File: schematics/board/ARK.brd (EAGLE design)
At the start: 89.6 x 89 mm, 199 parts, among them IC1 STM32F103C8T, Q5 8MHz

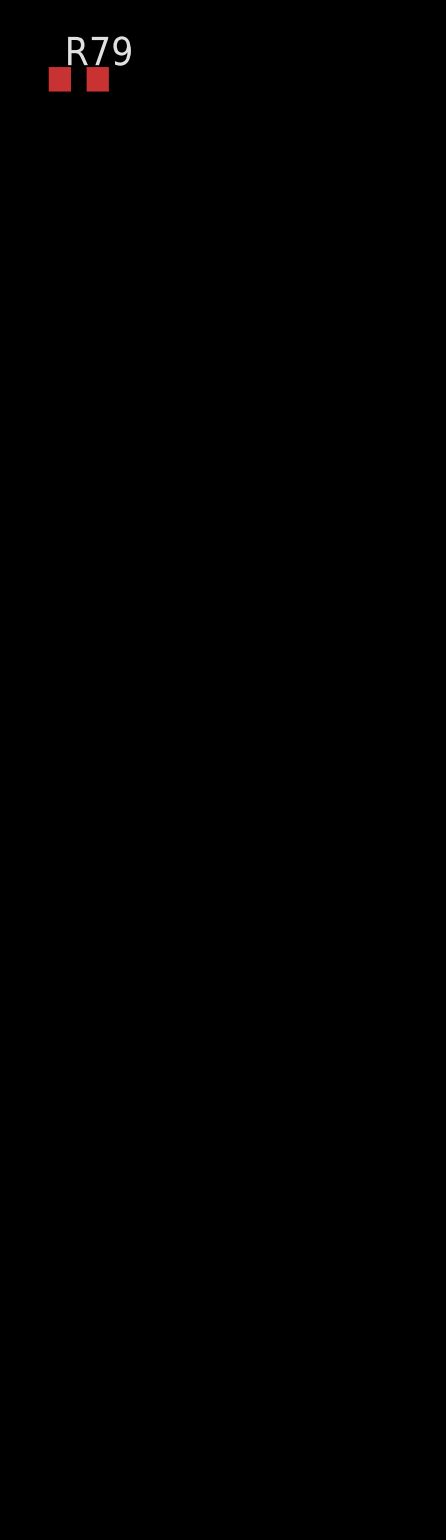
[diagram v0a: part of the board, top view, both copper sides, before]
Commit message: изменения схемы АРК
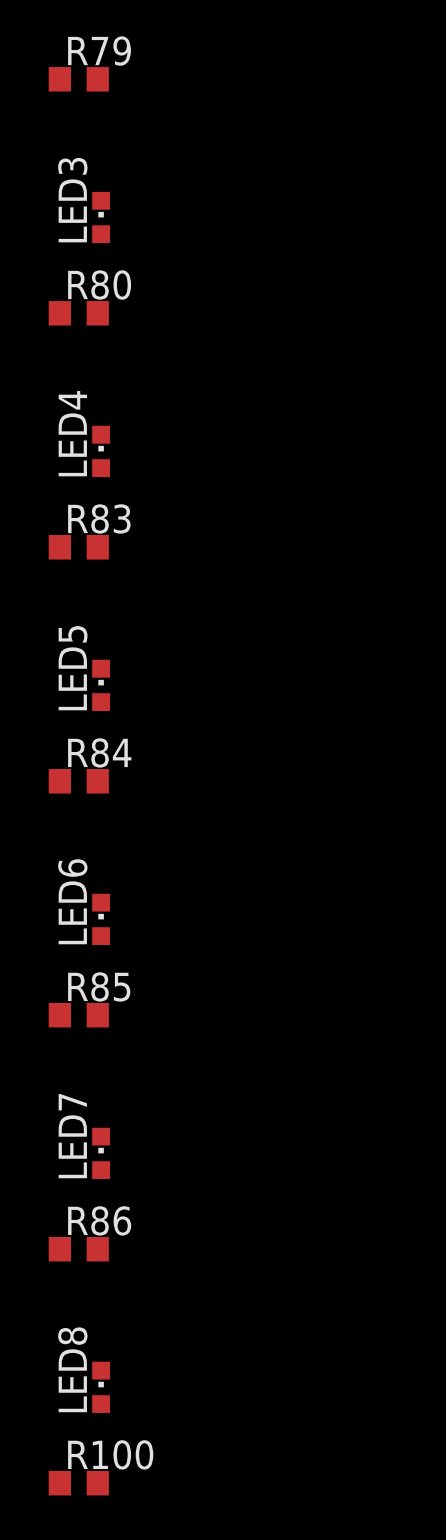
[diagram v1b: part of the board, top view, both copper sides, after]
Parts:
- added LED3, LED4, LED5, LED6, LED7, LED8: (no value), led:CHIPLED_0603
- added R100, R80, R83, R84, R85, R86: 1k2, resistor:R0603
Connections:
- net N$138 renamed 90
- new net N$25: R70.1, U$60.2
- new net N$5: R30.1, U$22.2
- new net N$54: LED3.A, R80.2
- new net N$56: LED4.A, R83.2
- new net N$57: LED5.A, R84.2
- new net N$58: LED6.A, R85.2
- new net N$59: LED7.A, R86.2
- new net N$60: LED8.A, R100.2
- net B-1: now also R86.1
- net B-2: now also R100.1
- net B-3: now also R84.1
- net B-4: now also R85.1
- net B-5: now also R83.1
- net B-6: now also R80.1
- net BUSPLUS: now also LED3.C, LED4.C, LED5.C, LED6.C, LED7.C, LED8.C
- net GND: now also U$22.10; no longer R30.1, R70.1, U$22.2, U$60.2
- net N$26: now also U$22.1
- net VDD: no longer U$22.1, U$22.10

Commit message: доработаны схемы БСК1 и БКУ
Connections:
- net GND: now also U$23.GND0, U$23.GND1; no longer U$23.P$12, U$23.P$9
- net RES-C: now also U$23.RESET/EN; no longer U$23.P$6
- net RX-C: now also U$23.RX0/M1; no longer U$23.P$11
- net SWC: now also U$23.SWC/TXD; no longer U$23.P$5
- net SWD: now also U$23.SWD/RXD; no longer U$23.P$4
- net TX-C: now also U$23.TX0/3V3; no longer U$23.P$10
- net VDD: now also U$23.3V3; no longer U$23.P$2, U$23.P$7
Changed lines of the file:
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@@
 <contactref element="VAR5B" pad="3"/>
 <contactref element="VAR5A" pad="3"/>
-<contactref element="U$23" pad="P$2"/>
-<contactref element="U$23" pad="P$7"/>
 <contactref element="R25" pad="1"/>
 <contactref element="R26" pad="1"/>
@@
 <contactref element="R64" pad="1"/>
 <contactref element="R79" pad="1"/>
+<contactref element="U$23" pad="3V3"/>
 <wire x1="40.69" y1="73.8" x2="65.69" y2="73.8" width="0" layer="19" extent="1-1"/>
 <wire x1="15.69" y1="73.8" x2="40.69" y2="73.8" width="0" layer="19" extent="1-1"/>
@@
 <wire x1="24.47" y1="25.1" x2="23.18" y2="40.7" width="0" layer="19" extent="1-1"/>
 <wire x1="41.31" y1="15.2" x2="24.47" y2="25.1" width="0" layer="19" extent="1-1"/>
-<wire x1="54.25" y1="12.1" x2="41.31" y2="15.2" width="0" layer="19" extent="1-1"/>
-<wire x1="56.75" y1="12.1" x2="54.25" y2="12.1" width="0" layer="19" extent="1-1"/>
-<wire x1="67.55" y1="14.65" x2="56.75" y2="12.1" width="0" layer="19" extent="1-1"/>
+<wire x1="54.75" y1="12.1" x2="41.31" y2="15.2" width="0" layer="19" extent="1-1"/>
+<wire x1="67.55" y1="14.65" x2="54.75" y2="12.1" width="0" layer="19" extent="1-1"/>
 <wire x1="73.05" y1="13.15" x2="67.55" y2="14.65" width="0" layer="19" extent="1-1"/>
 <wire x1="69.05" y1="21.65" x2="67.55" y2="14.65" width="0" layer="19" extent="1-1"/>
@@
 <wire x1="86.85" y1="18.9" x2="81.9" y2="25.55" width="0" layer="19" extent="1-1"/>
 <wire x1="86.85" y1="17.8" x2="86.85" y2="18.9" width="0" layer="19" extent="1-1"/>
-<wire x1="-24.7" y1="-300.97" x2="54.25" y2="12.1" width="0" layer="19" extent="1-1"/>
+<wire x1="-24.7" y1="-300.97" x2="41.31" y2="15.2" width="0" layer="19" extent="1-1"/>
 <wire x1="-28.7" y1="-300.97" x2="-24.7" y2="-300.97" width="0" layer="19" extent="1-1"/>
 <wire x1="-31.3" y1="-299.68" x2="-28.7" y2="-300.97" width="0" layer="19" extent="1-1"/>
@@
 <contactref element="R62" pad="1"/>
 <contactref element="R82" pad="1"/>
-<contactref element="U$23" pad="P$12" route="any" routetag="G$1.GND"/>
-<contactref element="U$23" pad="P$9" route="any" routetag="G$1.GND"/>
 <contactref element="U$24" pad="23"/>
 <contactref element="U$15" pad="23"/>
@@
 <contactref element="VAR5A" pad="4"/>
 <contactref element="U$22" pad="10"/>
+<contactref element="U$23" pad="GND0"/>
+<contactref element="U$23" pad="GND1"/>
 <wire x1="71.6" y1="55.4" x2="68.23" y2="73.8" width="0" layer="19" extent="1-1"/>
 <wire x1="59.3" y1="55.4" x2="71.6" y2="55.4" width="0" layer="19" extent="1-1"/>
@@
 <wire x1="18.23" y1="73.8" x2="21.6" y2="55.4" width="0" layer="19" extent="1-1"/>
 <wire x1="52.3" y1="12.1" x2="30.3" y2="19.8" width="0" layer="19" extent="1-1"/>
+<wire x1="58.7" y1="12.1" x2="52.3" y2="12.1" width="0" layer="19" extent="1-1"/>
 <wire x1="72.55" y1="13.15" x2="58.7" y2="12.1" width="0" layer="19" extent="1-1"/>
 <wire x1="71.7" y1="25.65" x2="72.55" y2="13.15" width="0" layer="19" extent="1-1"/>
@@
 </signal>
 <signal name="SWC">
-<contactref element="U$23" pad="P$5"/>
 <contactref element="IC1" pad="37"/>
 <contactref element="R27" pad="2"/>
+<contactref element="U$23" pad="SWC/TXD"/>
 <wire x1="67.55" y1="20.15" x2="81.9" y2="23.85" width="0" layer="19" extent="1-1"/>
 <wire x1="55.75" y1="12.1" x2="67.55" y2="20.15" width="0" layer="19" extent="1-1"/>
 </signal>
 <signal name="SWD">
-<contactref element="U$23" pad="P$4"/>
 <contactref element="IC1" pad="34"/>
 <contactref element="R64" pad="2"/>
+<contactref element="U$23" pad="SWD/RXD"/>
 <wire x1="70.05" y1="21.65" x2="81.9" y2="28.75" width="0" layer="19" extent="1-1"/>
 <wire x1="55.25" y1="12.1" x2="70.05" y2="21.65" width="0" layer="19" extent="1-1"/>
 </signal>
 <signal name="TX-C">
-<contactref element="U$23" pad="P$10"/>
 <contactref element="IC1" pad="30"/>
-<wire x1="53.1" y1="12.1" x2="72.05" y2="21.65" width="0" layer="19" extent="1-1"/>
+<contactref element="U$23" pad="TX0/3V3"/>
+<wire x1="57.25" y1="12.1" x2="72.05" y2="21.65" width="0" layer="19" extent="1-1"/>
 </signal>
 <signal name="RX-C">
-<contactref element="U$23" pad="P$11"/>
 <contactref element="IC1" pad="31"/>
-<wire x1="57.9" y1="12.1" x2="71.55" y2="21.65" width="0" layer="19" extent="1-1"/>
+<contactref element="U$23" pad="RX0/M1"/>
+<wire x1="53.75" y1="12.1" x2="71.55" y2="21.65" width="0" layer="19" extent="1-1"/>
 </signal>
 <signal name="RES-C">
-<contactref element="U$23" pad="P$6"/>
 <contactref element="IC1" pad="7"/>
 <contactref element="R79" pad="2"/>
-<wire x1="56.25" y1="12.1" x2="-54.15" y2="-330.9" width="0" layer="19" extent="1-1"/>
-<wire x1="72.05" y1="13.15" x2="56.25" y2="12.1" width="0" layer="19" extent="1-1"/>
+<contactref element="U$23" pad="RESET/EN"/>
+<wire x1="53.1" y1="12.1" x2="-54.15" y2="-330.9" width="0" layer="19" extent="1-1"/>
+<wire x1="72.05" y1="13.15" x2="53.1" y2="12.1" width="0" layer="19" extent="1-1"/>
 </signal>
 <signal name="N$5">

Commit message: обновлена схема БКУ
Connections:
- removed net RES-C: IC1.7, R79.2, U$23.RESET/EN
- new net NRST: IC1.7, R79.2, U$23.NRST/EN
- net RX-C: now also U$23.RX0; no longer U$23.RX0/M1
- net TX-C: now also U$23.TX0; no longer U$23.TX0/3V3
- net VDD: now also U$23.3V3/BUS0, U$23.3V3/BUS1; no longer U$23.3V3
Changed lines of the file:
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@@
 <contactref element="R64" pad="1"/>
 <contactref element="R79" pad="1"/>
-<contactref element="U$23" pad="3V3"/>
+<contactref element="U$23" pad="3V3/BUS1"/>
+<contactref element="U$23" pad="3V3/BUS0"/>
 <wire x1="40.69" y1="73.8" x2="65.69" y2="73.8" width="0" layer="19" extent="1-1"/>
 <wire x1="15.69" y1="73.8" x2="40.69" y2="73.8" width="0" layer="19" extent="1-1"/>
@@
 <wire x1="24.47" y1="25.1" x2="23.18" y2="40.7" width="0" layer="19" extent="1-1"/>
 <wire x1="41.31" y1="15.2" x2="24.47" y2="25.1" width="0" layer="19" extent="1-1"/>
-<wire x1="54.75" y1="12.1" x2="41.31" y2="15.2" width="0" layer="19" extent="1-1"/>
-<wire x1="67.55" y1="14.65" x2="54.75" y2="12.1" width="0" layer="19" extent="1-1"/>
+<wire x1="54.25" y1="12.1" x2="41.31" y2="15.2" width="0" layer="19" extent="1-1"/>
+<wire x1="56.75" y1="12.1" x2="54.25" y2="12.1" width="0" layer="19" extent="1-1"/>
+<wire x1="67.55" y1="14.65" x2="56.75" y2="12.1" width="0" layer="19" extent="1-1"/>
 <wire x1="73.05" y1="13.15" x2="67.55" y2="14.65" width="0" layer="19" extent="1-1"/>
 <wire x1="69.05" y1="21.65" x2="67.55" y2="14.65" width="0" layer="19" extent="1-1"/>
@@
 <wire x1="86.85" y1="18.9" x2="81.9" y2="25.55" width="0" layer="19" extent="1-1"/>
 <wire x1="86.85" y1="17.8" x2="86.85" y2="18.9" width="0" layer="19" extent="1-1"/>
-<wire x1="-24.7" y1="-300.97" x2="41.31" y2="15.2" width="0" layer="19" extent="1-1"/>
+<wire x1="-24.7" y1="-300.97" x2="54.25" y2="12.1" width="0" layer="19" extent="1-1"/>
 <wire x1="-28.7" y1="-300.97" x2="-24.7" y2="-300.97" width="0" layer="19" extent="1-1"/>
 <wire x1="-31.3" y1="-299.68" x2="-28.7" y2="-300.97" width="0" layer="19" extent="1-1"/>
@@
 <signal name="TX-C">
 <contactref element="IC1" pad="30"/>
-<contactref element="U$23" pad="TX0/3V3"/>
+<contactref element="U$23" pad="TX0"/>
 <wire x1="57.25" y1="12.1" x2="72.05" y2="21.65" width="0" layer="19" extent="1-1"/>
 </signal>
 <signal name="RX-C">
 <contactref element="IC1" pad="31"/>
-<contactref element="U$23" pad="RX0/M1"/>
+<contactref element="U$23" pad="RX0"/>
 <wire x1="53.75" y1="12.1" x2="71.55" y2="21.65" width="0" layer="19" extent="1-1"/>
 </signal>
-<signal name="RES-C">
+<signal name="NRST">
 <contactref element="IC1" pad="7"/>
 <contactref element="R79" pad="2"/>
-<contactref element="U$23" pad="RESET/EN"/>
+<contactref element="U$23" pad="NRST/EN"/>
 <wire x1="53.1" y1="12.1" x2="-54.15" y2="-330.9" width="0" layer="19" extent="1-1"/>
 <wire x1="72.05" y1="13.15" x2="53.1" y2="12.1" width="0" layer="19" extent="1-1"/>

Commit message: Добавлены светодиоды на платы БСК
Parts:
- added C32, C51: 0,1µ, rcl:C0603
- added C43, C52: 10µ, rcl:C1206
- C30, C36, C38: device rcl:C1206 -> rcl:C0603
- R30: value ? -> 150k
- R61: value ? -> 680k
- R70: value 51k -> 150k
- R83: value 1k2 -> 2k
- moved R100 409.9 mm to (18.5, 9.40), turned to 90 degrees
- moved LED8 405.8 mm to (14.2, 10.4), turned to 90 degrees
- moved R86 395.9 mm to (20.0, 5.30), turned to 90 degrees
- moved LED7 391.7 mm to (15.7, 6.30), turned to 90 degrees
- moved R63 386.4 mm to (75.2, 37.8), turned to 180 degrees
- moved R85 381.6 mm to (12.3, 2.70), turned to 90 degrees
- moved R84 380.1 mm to (27.9, 8.50), turned to 90 degrees
- moved LED6 377.4 mm to (8.00, 3.70), turned to 90 degrees
- moved LED5 375.7 mm to (23.6, 9.50), turned to 90 degrees
- moved R79 370.6 mm to (78.4, 14.9)
- moved R32 365.5 mm to (67.7, 45.0), turned to 180 degrees
- moved R83 364.1 mm to (8.60, 6.60), turned to 90 degrees
- moved LED4 360.0 mm to (4.30, 7.60), turned to 90 degrees
- moved R57 358.2 mm to (67.7, 39.0), turned to 180 degrees
- moved R80 357.7 mm to (9.00, 10.5), turned to 90 degrees
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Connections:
- removed net N$26: C31.1, U$16.11, U$16.15, U$16.16, U$22.1
- removed net RESET: IC1.28, U$22.7, U$60.7
- new net DPC_RST: IC1.27, U$60.7
- new net DPD_RST: IC1.28, U$22.7
- net BUSPLUS: no longer LED4.C
- net GND: now also C32.2, C43.2, C51.2, C52.2
- net N$25: now also C32.1, C43.1, U$60.1
- net N$5: now also C51.1, C52.1, U$22.1
- net VDD: now also C31.1, LED4.C, U$16.11, U$16.15, U$16.16; no longer U$60.1

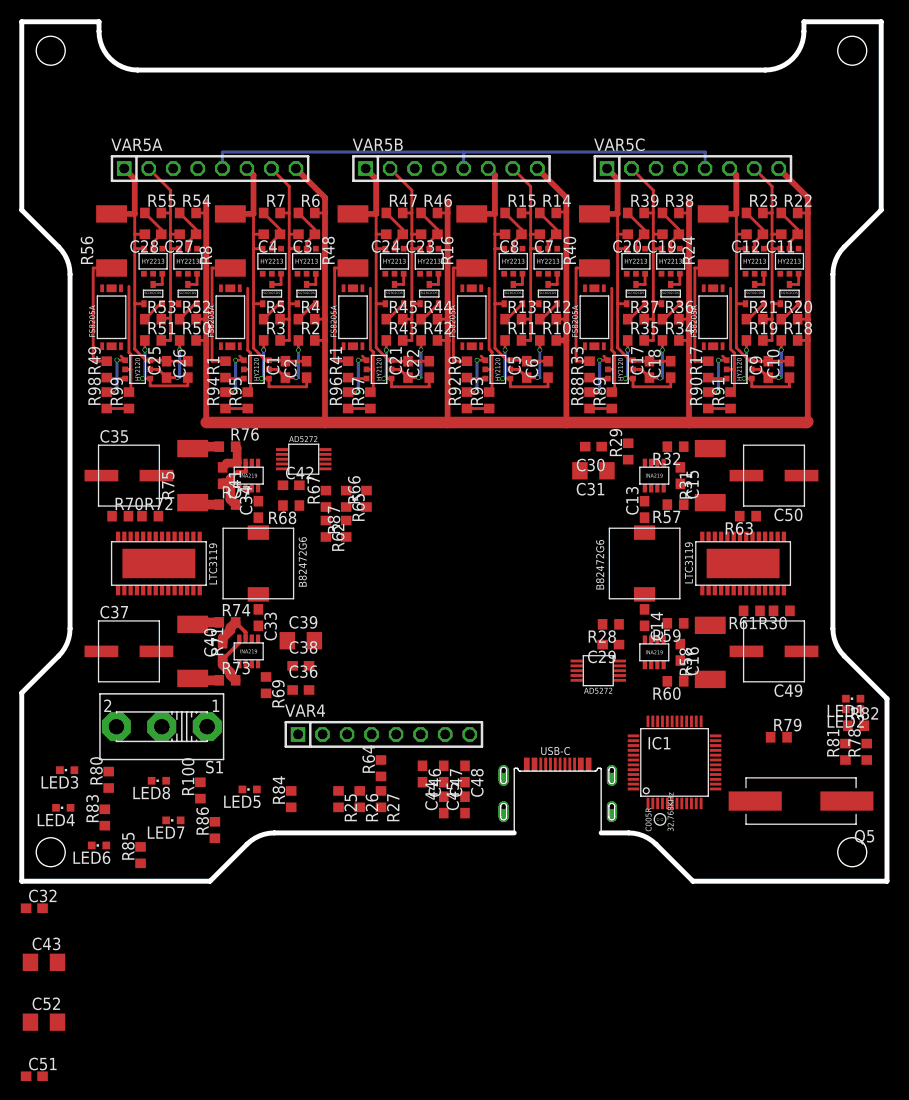
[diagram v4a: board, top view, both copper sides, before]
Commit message: Незначительные изменения в платах БСК1 и АРК
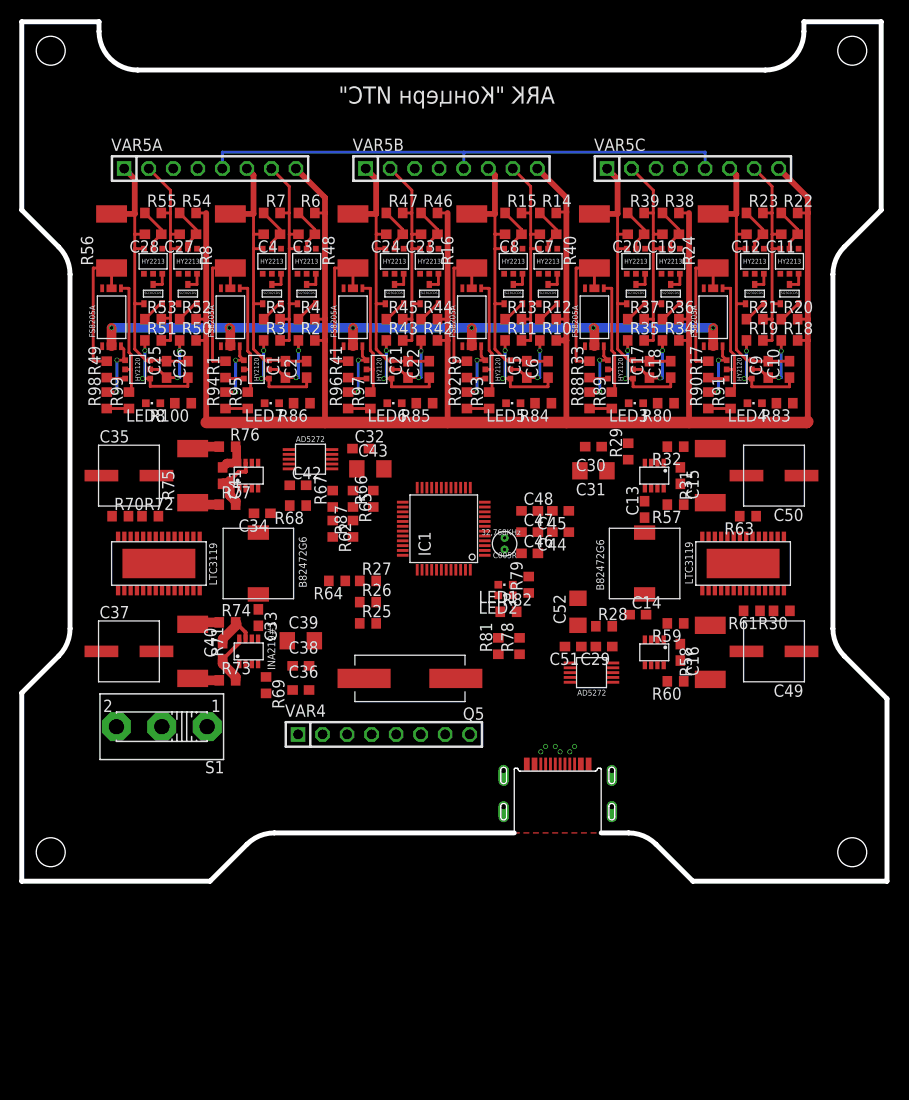
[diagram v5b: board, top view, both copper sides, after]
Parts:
- R100, R80, R84, R85, R86: value 1k2 -> 2k
- moved LED4 83.0 mm to (75.9, 49.5)
- moved R83 82.4 mm to (79.0, 49.5), turned to 180 degrees
- moved C51 71.4 mm to (57.1, 24.3), turned to 180 degrees
- moved LED3 70.1 mm to (63.6, 49.5)
- moved C52 69.7 mm to (57.6, 27.9), turned to 90 degrees
- moved R80 69.6 mm to (66.7, 49.5), turned to 180 degrees
- moved C43 61.3 mm to (36.1, 42.7)
- moved C32 58.4 mm to (35.1, 44.8)
- moved R85 55.3 mm to (41.7, 49.5), turned to 180 degrees
- moved LED6 55.1 mm to (38.6, 49.5)
- moved R84 48.6 mm to (54.0, 49.5), turned to 180 degrees
- moved LED5 48.4 mm to (50.9, 49.5)
- moved R86 45.1 mm to (29.0, 49.5), turned to 180 degrees
- moved LED7 44.4 mm to (25.9, 49.5)
- moved Q5 42.4 mm to (40.2, 21.0)
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- renumbered U$58 to INA219#1
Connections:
- net BUSPLUS: now also LED4.C
- net VDD: no longer LED4.C
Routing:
- net GND: track 0.00 -> 73.8 mm, vias 0 -> 6
- net BMS+: track 235.3 -> 231.8 mm
- net N$88: track 12.9 -> 15.0 mm
- net N$72: track 12.9 -> 15.0 mm
- net N$104: track 12.9 -> 15.1 mm
- net N$13: track 12.9 -> 14.9 mm
- net N$24: track 12.9 -> 14.9 mm
- net N$40: track 12.9 -> 14.8 mm
- net OD6: track 5.80 -> 6.83 mm
- net OD5: track 5.80 -> 6.83 mm
- net OD4: track 5.80 -> 6.83 mm
- net OD3: track 5.80 -> 6.83 mm
- net OD2: track 5.83 -> 6.86 mm
- net OD1: track 5.80 -> 6.83 mm
- net OC5: track 11.9 -> 12.7 mm
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- added copper zone on layer 1, net GND
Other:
- board text added: "ARK "Концерн ИТС""
